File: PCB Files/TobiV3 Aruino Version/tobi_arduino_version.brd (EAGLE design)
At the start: 103 x 74 mm, 45 parts

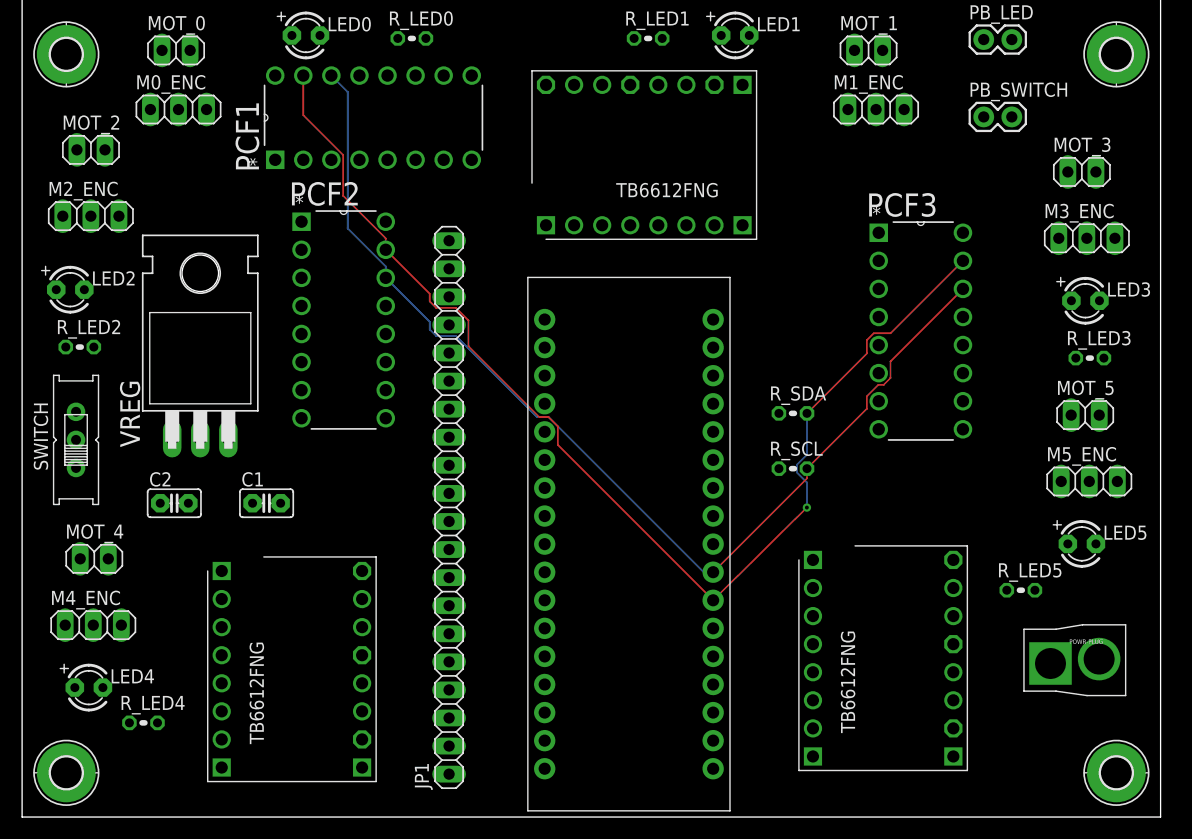
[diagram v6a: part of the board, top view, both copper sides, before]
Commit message: hand route sda/scl and thick traces for motor voltage
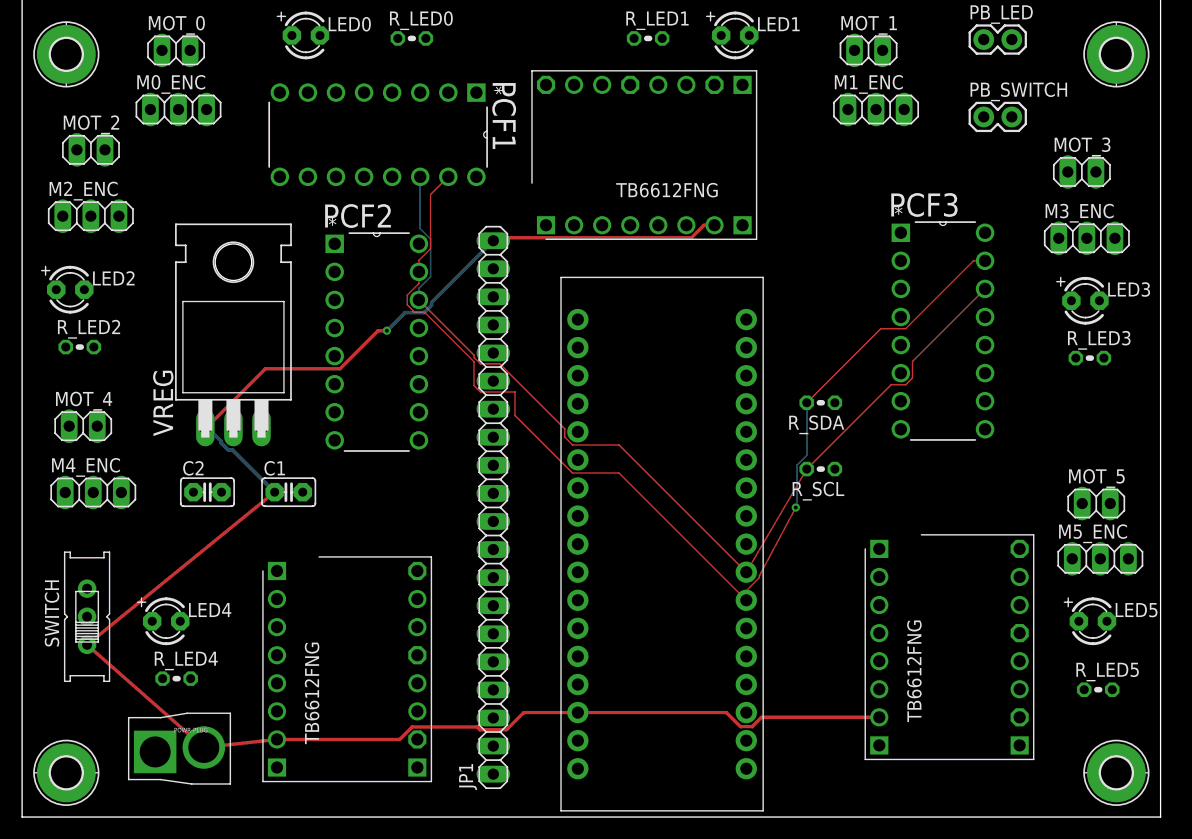
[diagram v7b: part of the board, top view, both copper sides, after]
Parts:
- moved POWR-PLUG 81.4 mm to (10.7, 12.4)
- moved PCF1 19.6 mm to (20.3, 63.9), turned to 270 degrees
- moved SWITCH 16.0 mm to (2.88, 24.1)
- moved MOT_4 12.0 mm to (2.53, 41.4)
- moved M4_ENC 12.0 mm to (3.44, 35.4)
- moved R_LED5 11.4 mm to (94.4, 17.5)
- moved LED4 9.22 mm to (10.0, 23.7)
- moved MOT_5 8.06 mm to (94.2, 34.4)
- moved LED5 7.07 mm to (93.9, 23.7)
- moved M5_ENC 7.07 mm to (94.5, 29.4)
- moved DRIVER3 6.08 mm to (73.3, 11.2)
- moved DRIVER2 5.00 mm to (18.8, 9.21)
- moved R_LED4 5.00 mm to (11.0, 18.5)
- moved JP1 4.00 mm to (39.6, 34.0)
- moved PCF2 3.61 mm to (32.9, 40.1)
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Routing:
- net V_MOT: track 0.00 -> 163.6 mm, vias 0 -> 1
- net SCL: track 96.7 -> 86.9 mm
- net SDA: track 106.1 -> 98.4 mm

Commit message: hand route gnd
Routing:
- net GND: track 0.00 -> 254.4 mm, vias 0 -> 5
- net SCL: track 86.9 -> 87.3 mm, vias 0 -> 1
